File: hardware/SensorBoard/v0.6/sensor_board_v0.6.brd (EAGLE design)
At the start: 46.8 x 39.9 mm, 48 parts, among them J3 USB-MICROB, U1 ATMEGA328P, U10 CCS811, U11 RFM69HW, U2 TSL2561, U4 MPL115A, U5 FT231XS, U7 SHT31, U8 MCP1703/3.3V, U9 MCP1703CB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

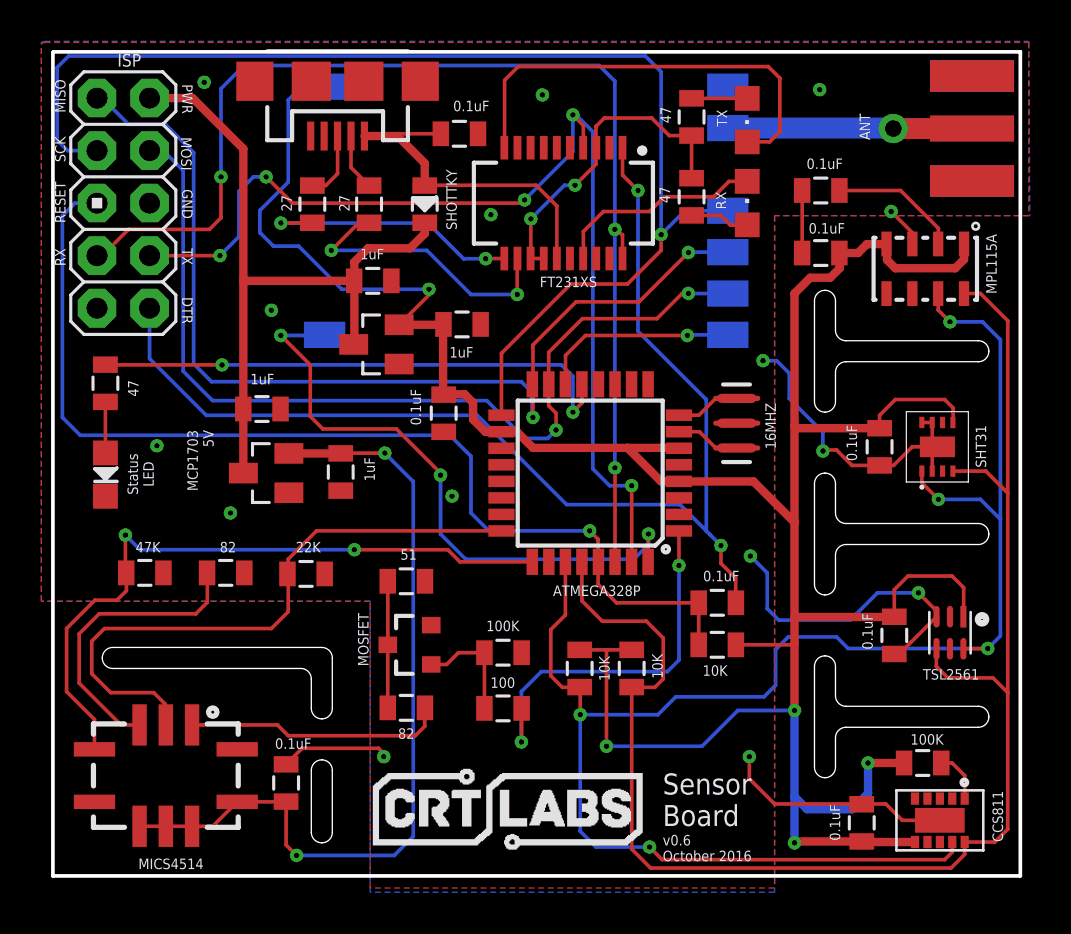
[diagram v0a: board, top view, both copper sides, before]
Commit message: Minor fixes to sensor board v0.6
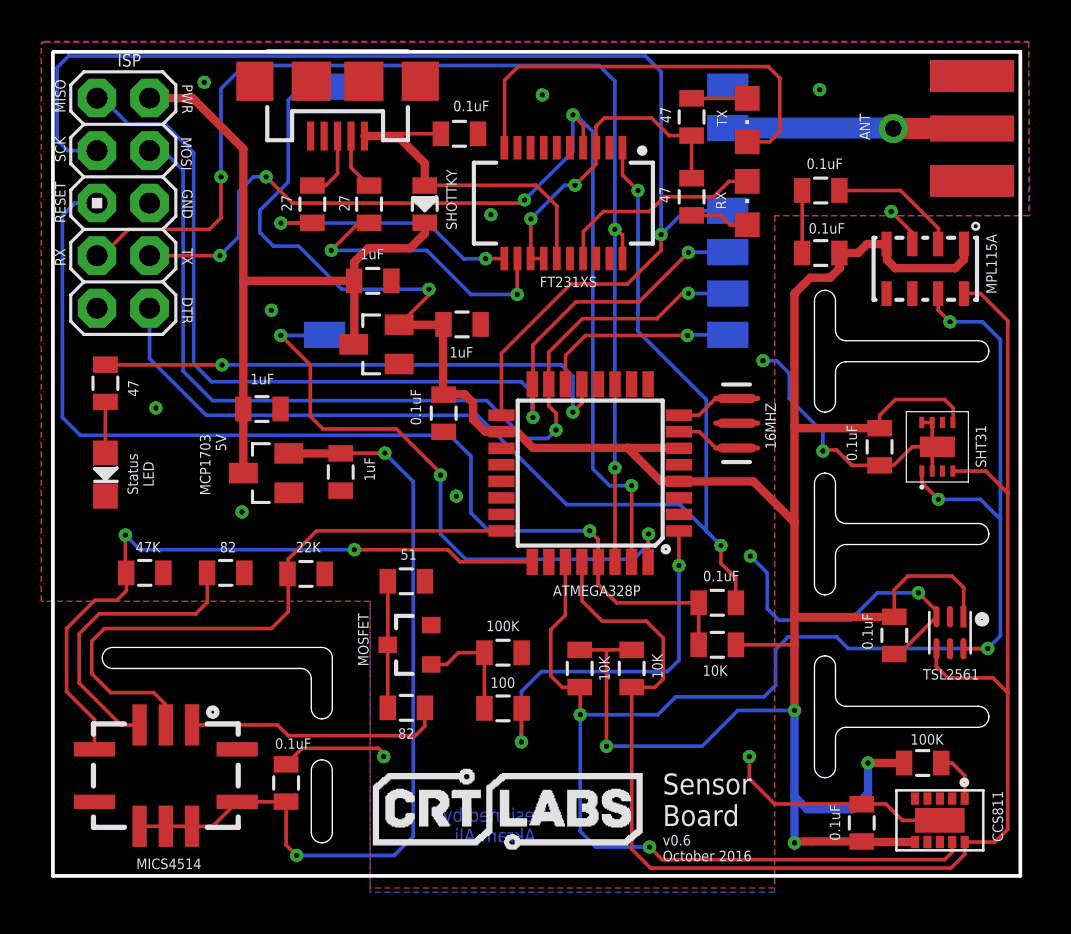
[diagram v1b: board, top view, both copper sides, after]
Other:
- board text added: "Designed by Akram Ali"
- board text removed: "Designed by Akram Ali and Dave Conroy"
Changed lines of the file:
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@@
 <wire x1="52.6796" y1="6.6294" x2="5.8928" y2="6.6294" width="0.1778" layer="20"/>
 <wire x1="5.8928" y1="6.6294" x2="5.8928" y2="46.4566" width="0.1778" layer="20"/>
-<text x="41.2496" y="9.7028" size="0.6096" layer="122" font="vector" rot="MR0">Designed by Akram Ali and Dave Conroy</text>
+<text x="27.2796" y="9.906" size="0.6604" layer="16" font="vector" ratio="14" rot="MR180" align="bottom-center">Designed by
+Akram Ali</text>
 <text x="35.3822" y="7.3406" size="0.508" layer="121" font="vector">v0.6
 October 2016</text>
-<text x="41.1988" y="8.128" size="1.27" layer="122" font="vector" ratio="10" rot="MR0">crtlabs.org</text>
+<text x="8.89" y="31.9532" size="1.27" layer="122" font="vector" ratio="10" rot="MR270">crtlabs.org</text>
 <rectangle x1="27.9146" y1="7.8994" x2="28.321" y2="7.9502" layer="121"/>
 <rectangle x1="27.813" y1="7.9502" x2="28.3718" y2="8.001" layer="121"/>
@@
 <text x="10.7696" y="26.0604" size="0.508" layer="121" font="vector" rot="SR90" align="bottom-center">Status
 LED</text>
-<text x="13.6652" y="28.194" size="0.508" layer="121" font="vector" rot="SR90" align="bottom-right">MCP1703
+<text x="14.2748" y="27.9908" size="0.508" layer="121" font="vector" rot="SR90" align="bottom-right">MCP1703
 5V</text>
 <text x="6.5024" y="43.5356" size="0.508" layer="121" font="vector" rot="R90">MISO</text>
@@
 <element name="MICS4514" library="MICS-4514_CO_and_NOx_Sensor_Breakout" package="SPARKFUN-SENSORS_MICS_10-SMD" value="SPARKFUN-SENSORS_MICS-4514" x="11.3538" y="11.4808" smashed="yes">
 <attribute name="PROD_ID" value="COMP-12310" x="11.3538" y="11.4808" size="1.778" layer="27" display="off"/>
-<attribute name="NAME" x="13.1826" y="7.4676" size="0.508" layer="121" font="vector" rot="R180"/>
+<attribute name="NAME" x="13.081" y="7.4676" size="0.508" layer="121" font="vector" rot="R180"/>
 </element>
 <element name="R14" library="SparkFun-Passives" package="0805" value="47K" x="10.3378" y="21.2852" smashed="yes" rot="R180">
@@
 </element>
 <element name="U11" library="RFM69 USB Gateway" package="LOWPOWERLAB_RFM69W-MINPADS" value="RFM69HW" x="30.5308" y="37.7952" smashed="yes" rot="MR180">
-<attribute name="VALUE" x="29.8276" y="46.242" size="0.508" layer="122" font="vector" rot="MR0"/>
+<attribute name="VALUE" x="30.488" y="30.9512" size="0.508" layer="122" font="vector" rot="MR0"/>
 </element>
 <element name="X1" library="adafruit" package="SMA_EDGELAUNCH" value="" x="52.3748" y="42.7736" smashed="yes" rot="R180">
@@
 <via x="29.5656" y="44.3992" extent="1-16" drill="0.254" diameter="0.127"/>
 <via x="46.4312" y="38.7604" extent="1-16" drill="0.254" diameter="0.127"/>
-<via x="14.478" y="24.1808" extent="1-16" drill="0.254" diameter="0.127"/>
+<via x="15.0368" y="24.2316" extent="1-16" drill="0.254" diameter="0.127"/>
 <via x="13.208" y="45.0088" extent="1-16" drill="0.254" diameter="0.127"/>
 <via x="16.4592" y="33.9852" extent="1-16" drill="0.254" diameter="0.127"/>
-<via x="25.1968" y="24.9936" extent="1-16" drill="0.254" diameter="0.127"/>
+<via x="25.4" y="24.9936" extent="1-16" drill="0.254" diameter="0.127"/>
 <via x="27.0764" y="38.608" extent="1-16" drill="0.254" diameter="0.127"/>
 <wire x1="45.0232" y1="10.1092" x2="40.7924" y2="10.1092" width="0.1778" layer="1"/>
@@
 <wire x1="46.824" y1="17.3626" x2="48.626" y2="19.1646" width="0.1778" layer="1"/>
 <wire x1="42.1276" y1="36.7538" x2="42.1276" y2="39.7764" width="0.1778" layer="1"/>
-<via x="10.922" y="27.432" extent="1-16" drill="0.254" diameter="0.127"/>
+<via x="10.8712" y="29.2608" extent="1-16" drill="0.254" diameter="0.127"/>
 <wire x1="48.626" y1="19.1646" x2="48.626" y2="19.446" width="0.1778" layer="1"/>
 <wire x1="48.626" y1="19.446" x2="47.752" y2="20.32" width="0.1778" layer="1"/>

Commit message: Silkscreen adjustments
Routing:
- net SDA: track 82.0 -> 83.9 mm
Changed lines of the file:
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@@
 <attribute name="MF" value="" x="48.6664" y="27.3812" size="1.778" layer="27" rot="R90" display="off"/>
 <attribute name="MPN" value="SHT31-DIS-B" x="48.6664" y="27.3812" size="1.778" layer="27" rot="R90" display="off"/>
-<attribute name="VALUE" x="50.7728" y="27.3988" size="0.508" layer="121" font="vector" rot="R90" align="center"/>
+<attribute name="VALUE" x="51.8396" y="27.3988" size="0.508" layer="121" font="vector" rot="R90" align="center"/>
 </element>
 <element name="U1" library="SparkFun-DigitalIC" package="TQFP32-08" value="ATMEGA328P" x="31.877" y="26.1112" smashed="yes" rot="R180">
@@
 <attribute name="MF" value="" x="49.276" y="18.3896" size="1.778" layer="27" rot="R270" display="off"/>
 <attribute name="MPN" value="TSL2561FN" x="49.276" y="18.3896" size="1.778" layer="27" rot="R270" display="off"/>
-<attribute name="VALUE" x="49.3268" y="16.6316" size="0.508" layer="121" font="vector" rot="R180" align="bottom-center"/>
+<attribute name="VALUE" x="51.5928" y="18.542" size="0.508" layer="121" font="vector" rot="R270" align="bottom-center"/>
 </element>
 <element name="R4" library="SparkFun-Resistors" package="0805" value="47" x="8.4328" y="30.4546" smashed="yes" rot="R270">
@@
 </element>
 <element name="U4" library="SparkFun-Sensors" package="LGA8" value="MPL115A" x="48.0822" y="35.9918" smashed="yes" rot="R270">
-<attribute name="VALUE" x="51.0286" y="37.6682" size="0.508" layer="121" font="vector" rot="R270"/>
+<attribute name="VALUE" x="51.5874" y="37.5158" size="0.508" layer="121" font="vector" rot="R270"/>
 </element>
 <element name="C13" library="SparkFun-Passives" package="0805" value="0.1uF" x="43.0276" y="39.7764" smashed="yes" rot="R180">
@@
 <element name="MICS4514" library="MICS-4514_CO_and_NOx_Sensor_Breakout" package="SPARKFUN-SENSORS_MICS_10-SMD" value="SPARKFUN-SENSORS_MICS-4514" x="11.3538" y="11.4808" smashed="yes">
 <attribute name="PROD_ID" value="COMP-12310" x="11.3538" y="11.4808" size="1.778" layer="27" display="off"/>
-<attribute name="NAME" x="13.081" y="7.4676" size="0.508" layer="121" font="vector" rot="R180"/>
+<attribute name="NAME" x="13.081" y="7.4168" size="0.508" layer="121" font="vector" rot="R180"/>
 </element>
 <element name="R14" library="SparkFun-Passives" package="0805" value="47K" x="10.3378" y="21.2852" smashed="yes" rot="R180">
@@
 </element>
 <element name="U10" library="CCS811" package="LGA" value="CCS811" x="46.7868" y="10.668" smashed="yes" rot="R270">
-<attribute name="VALUE" x="51.3334" y="10.7442" size="0.508" layer="121" font="vector" rot="R270"/>
+<attribute name="VALUE" x="51.5874" y="10.7442" size="0.508" layer="121" font="vector" rot="R270"/>
 </element>
 <element name="C5" library="SparkFun-Passives" package="0805" value="0.1uF" x="45.0088" y="9.1948" smashed="yes" rot="R90">
@@
 <wire x1="49.9868" y1="8.268" x2="51.448" y2="8.268" width="0.1778" layer="1"/>
 <wire x1="51.448" y1="8.268" x2="52.07" y2="8.89" width="0.1778" layer="1"/>
-<wire x1="52.07" y1="8.89" x2="52.07" y2="15.494" width="0.1778" layer="1"/>
-<wire x1="52.07" y1="15.494" x2="51.3588" y2="16.2052" width="0.1778" layer="1"/>
-<wire x1="51.3588" y1="16.2052" x2="49.1744" y2="16.2052" width="0.1778" layer="1"/>
-<wire x1="49.1744" y1="16.2052" x2="48.6156" y2="16.764" width="0.1778" layer="1"/>
-<wire x1="48.6156" y1="16.764" x2="48.6156" y2="17.6042" width="0.1778" layer="1"/>
 <wire x1="48.6156" y1="17.6042" x2="48.626" y2="17.6146" width="0.1778" layer="1"/>
 <wire x1="49.4164" y1="26.2062" x2="51.0098" y2="26.2062" width="0.1778" layer="1"/>
 <wire x1="51.0098" y1="26.2062" x2="52.07" y2="25.146" width="0.1778" layer="1"/>
+<wire x1="52.07" y1="8.89" x2="52.07" y2="15.494" width="0.1778" layer="1"/>
 <wire x1="52.07" y1="15.494" x2="52.07" y2="25.146" width="0.1778" layer="1"/>
 <wire x1="52.07" y1="25.146" x2="52.07" y2="33.4772" width="0.1778" layer="1"/>
@@
 <wire x1="49.9868" y1="7.6704" x2="49.3268" y2="7.0104" width="0.1778" layer="1"/>
 <wire x1="49.3268" y1="7.0104" x2="34.798" y2="7.0104" width="0.1778" layer="1"/>
+<wire x1="48.6156" y1="17.6042" x2="48.6156" y2="16.2052" width="0.1778" layer="1"/>
+<wire x1="48.6156" y1="16.2052" x2="49.3268" y2="15.494" width="0.1778" layer="1"/>
+<wire x1="49.3268" y1="15.494" x2="52.07" y2="15.494" width="0.1778" layer="1"/>
 </signal>
 <signal name="SDA">
@@
 <wire x1="31.3944" y1="14.4272" x2="31.3944" y2="15.737" width="0.1778" layer="1"/>
 <wire x1="31.3944" y1="15.737" x2="31.369" y2="15.7624" width="0.1778" layer="1"/>
-<wire x1="49.926" y1="17.6146" x2="51.0918" y2="17.6146" width="0.1778" layer="1"/>
-<wire x1="51.0918" y1="17.6146" x2="51.1048" y2="17.6276" width="0.1778" layer="1"/>
-<via x="51.1048" y="17.6276" extent="1-16" drill="0.254" diameter="0.127"/>
-<wire x1="51.1048" y1="17.6276" x2="44.3484" y2="17.6276" width="0.1778" layer="16"/>
+<via x="50.292" y="16.2052" extent="1-16" drill="0.254" diameter="0.127"/>
 <wire x1="44.3484" y1="17.6276" x2="43.7896" y2="18.1864" width="0.1778" layer="16"/>
 <wire x1="40.8432" y1="17.5768" x2="41.4528" y2="18.1864" width="0.1778" layer="16"/>
@@
 <wire x1="48.7172" y1="24.8412" x2="50.7492" y2="24.8412" width="0.1778" layer="16"/>
 <wire x1="50.7492" y1="24.8412" x2="51.7144" y2="23.876" width="0.1778" layer="16"/>
-<wire x1="51.7144" y1="23.876" x2="51.7144" y2="18.2372" width="0.1778" layer="16"/>
-<wire x1="51.7144" y1="18.2372" x2="51.1048" y2="17.6276" width="0.1778" layer="16"/>
+<wire x1="51.7144" y1="23.876" x2="51.7144" y2="17.6276" width="0.1778" layer="16"/>
 <wire x1="48.7072" y1="34.7918" x2="48.7072" y2="33.9952" width="0.1778" layer="1"/>
 <wire x1="48.7072" y1="33.9952" x2="49.276" y2="33.4264" width="0.1778" layer="1"/>
@@
 <wire x1="36.0172" y1="15.2908" x2="35.1536" y2="14.4272" width="0.1778" layer="16"/>
 <wire x1="35.1536" y1="14.4272" x2="31.3944" y2="14.4272" width="0.1778" layer="16"/>
+<wire x1="51.7144" y1="17.6276" x2="50.292" y2="16.2052" width="0.1778" layer="16"/>
+<wire x1="49.926" y1="17.6146" x2="49.926" y2="16.5712" width="0.1778" layer="1"/>
+<wire x1="49.926" y1="16.5712" x2="50.292" y2="16.2052" width="0.1778" layer="1"/>
+<wire x1="44.3484" y1="17.6276" x2="48.8696" y2="17.6276" width="0.1778" layer="16"/>
+<wire x1="48.8696" y1="17.6276" x2="50.292" y2="16.2052" width="0.1778" layer="16"/>
 </signal>
 <signal name="D5">

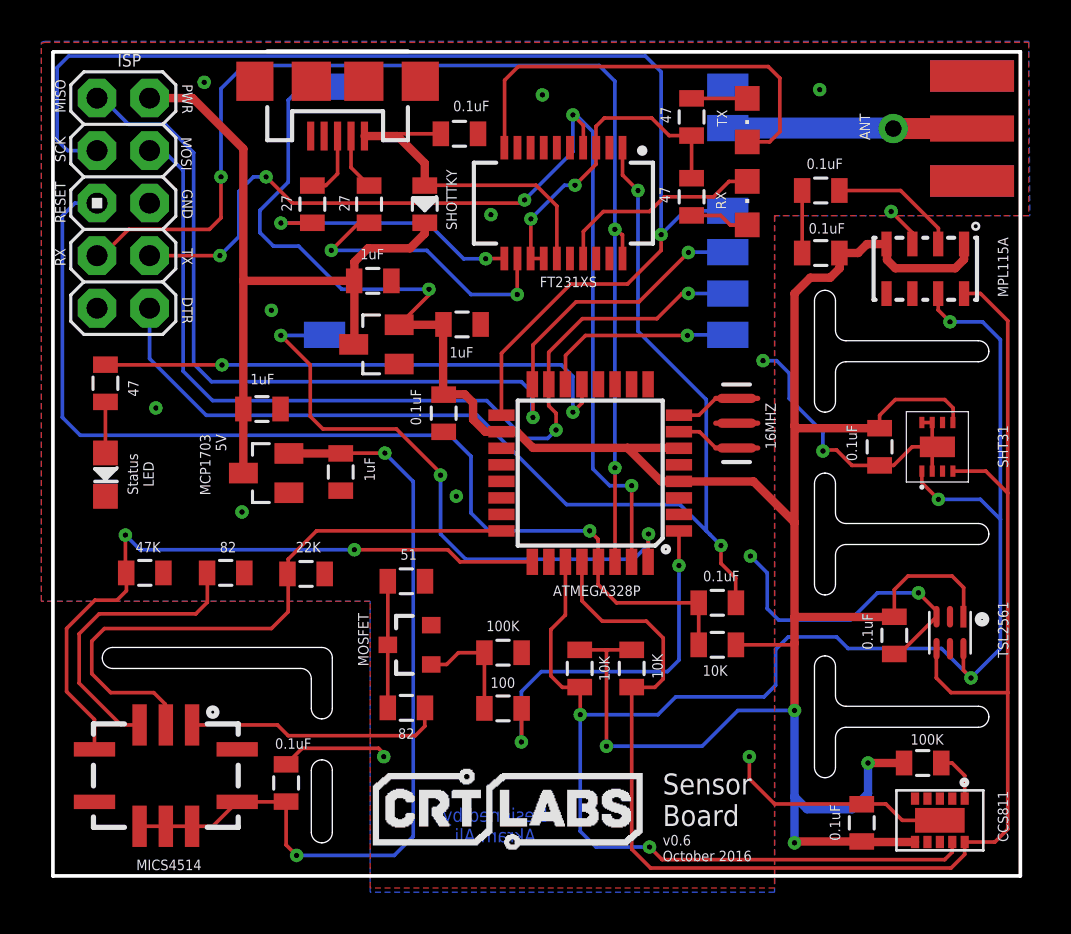
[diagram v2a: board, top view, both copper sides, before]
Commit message: Added environmental parameters to silkscreen
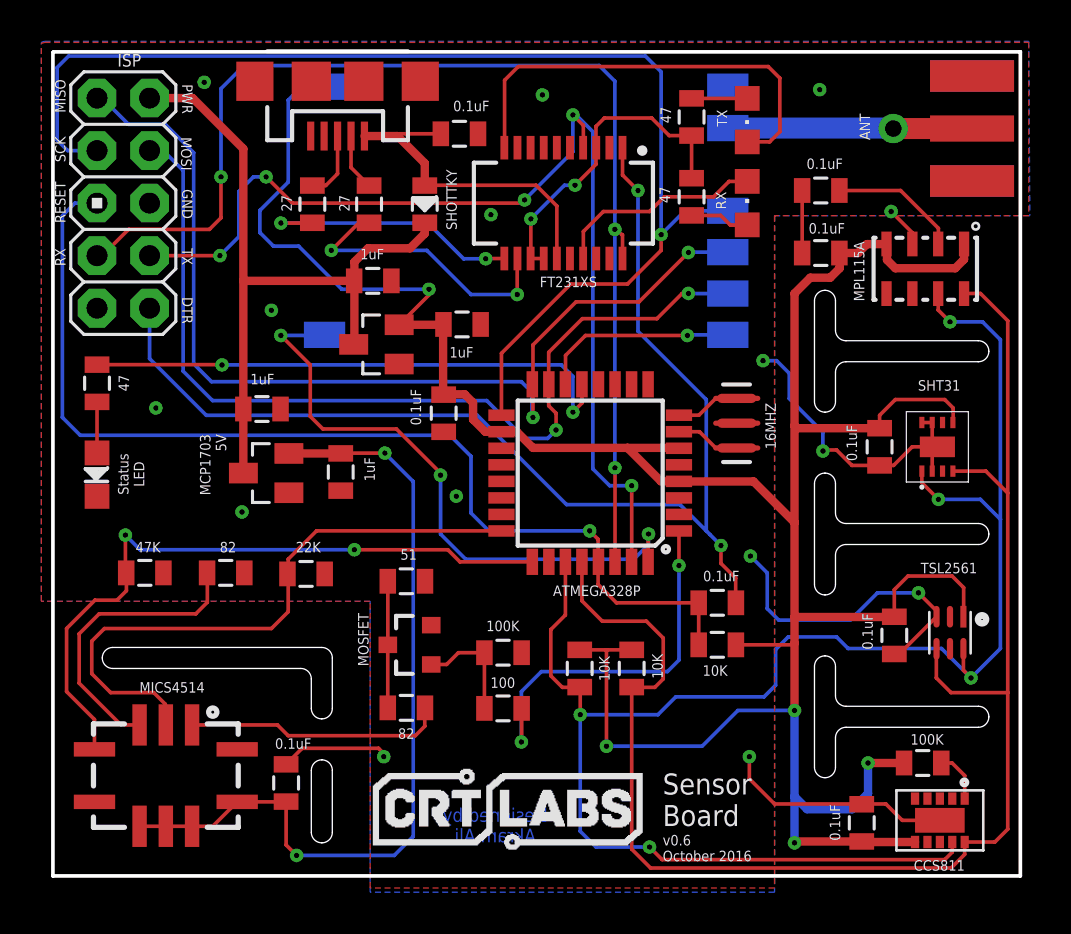
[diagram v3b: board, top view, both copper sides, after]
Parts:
- moved LED2 0.41 mm to (8.03, 26.0)
- moved R4 0.41 mm to (8.03, 30.5)
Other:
- board text added: "AIr Pressure"
- board text added: "CO / NO2"
- board text added: "Light"
- board text added: "Temperature Humidity"
- board text added: "VOC / CO2"
